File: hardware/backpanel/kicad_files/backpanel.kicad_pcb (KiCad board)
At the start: 2 copper layers, 72 x 19.2 mm, 0 parts

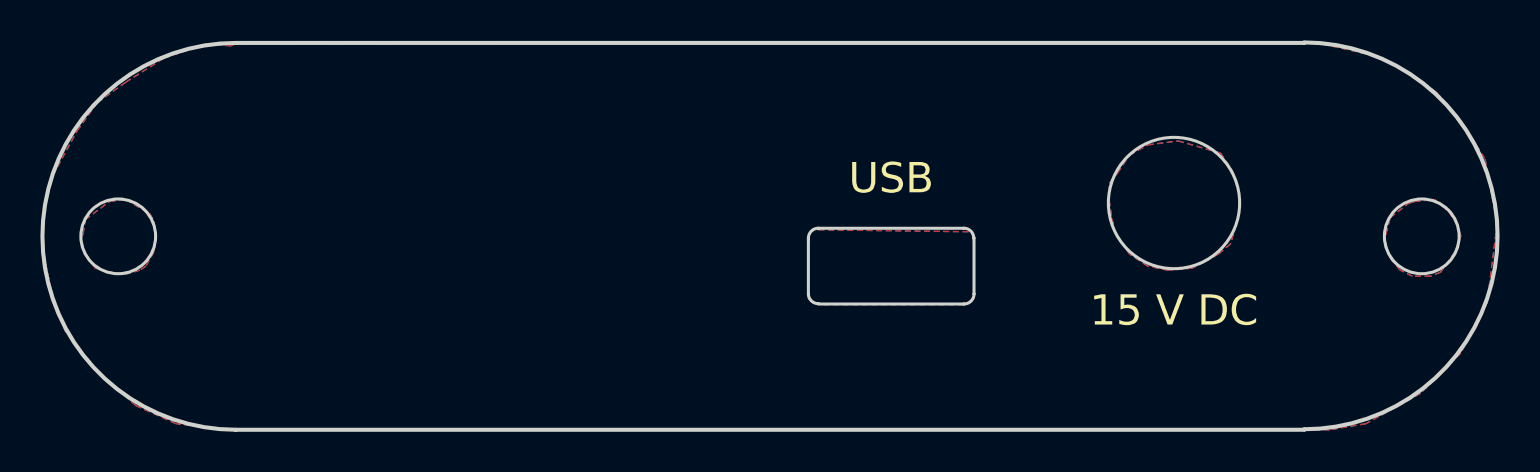
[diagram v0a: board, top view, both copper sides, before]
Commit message: Add files via upload
minor changes to allow KiCad design rules check to complete without errors or warnings
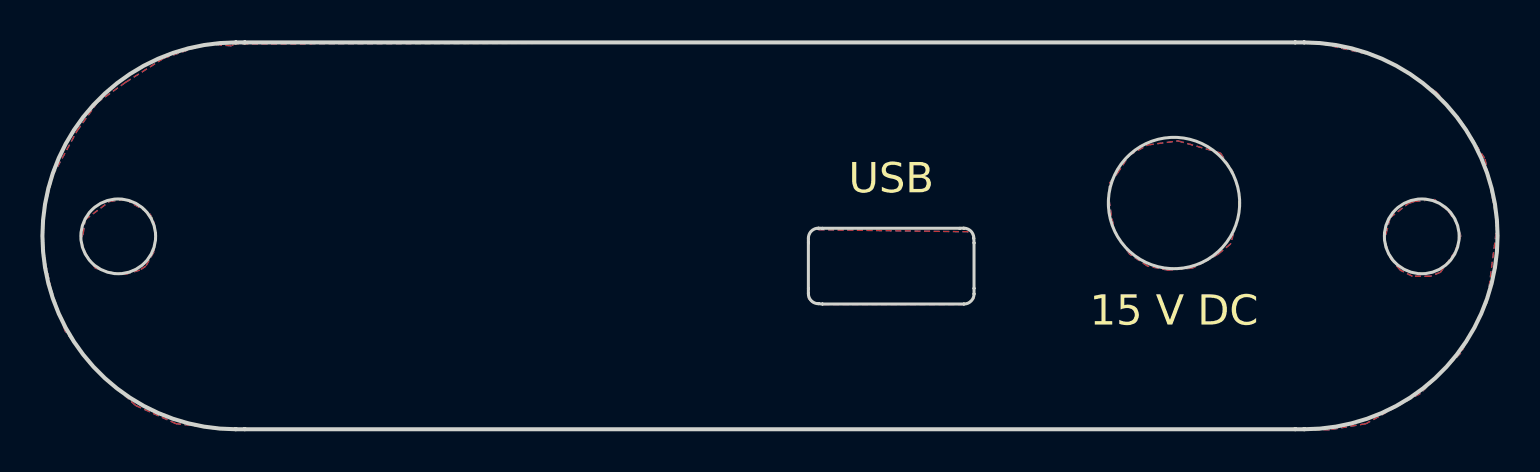
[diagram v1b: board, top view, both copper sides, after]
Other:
- board size 72 x 19.2 mm -> 72 x 19.1 mm
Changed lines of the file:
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@@
   )
   (net 0 "")
-  (gr_arc (start 123.557 100) (mid 113.982 90.425) (end 123.557 80.85) (layer "Edge.Cuts") (width 0.2))
-  (gr_line (start 160.1 90.5) (end 160.1 93.275) (layer "Edge.Cuts") (width 0.15))
-  (gr_line (start 152.4 93.775) (end 159.6 93.775) (layer "Edge.Cuts") (width 0.15))
+  (gr_arc (start 123.557 99.975) (mid 113.982 90.4) (end 123.557 80.825) (layer "Edge.Cuts") (width 0.2))
+  (gr_line (start 160.1 90.75) (end 160.1 93) (layer "Edge.Cuts") (width 0.15))
+  (gr_line (start 152.6 93.775) (end 159.6 93.775) (layer "Edge.Cuts") (width 0.15))
   (gr_arc (start 151.9 90.52) (mid 152.046447 90.166447) (end 152.4 90.02) (layer "Edge.Cuts") (width 0.15))
   (gr_arc (start 152.4 93.76) (mid 152.046447 93.613553) (end 151.9 93.26) (layer "Edge.Cuts") (width 0.15))
   (gr_arc (start 160.1 93.275) (mid 159.953553 93.628553) (end 159.6 93.775) (layer "Edge.Cuts") (width 0.15))
+  (gr_line (start 151.9 93) (end 151.9 93.26) (layer "Edge.Cuts") (width 0.15))
+  (gr_line (start 151.9 90.75) (end 151.9 90.52) (layer "Edge.Cuts") (width 0.15))
   (gr_arc (start 159.59 90.02) (mid 159.943553 90.166447) (end 160.09 90.52) (layer "Edge.Cuts") (width 0.15))
+  (gr_line (start 152.4 90.02) (end 152.6 90.025) (layer "Edge.Cuts") (width 0.15))
+  (gr_line (start 160.09 90.52) (end 160.1 90.75) (layer "Edge.Cuts") (width 0.15))
+  (gr_line (start 176 99.975) (end 176.443 99.975) (layer "Edge.Cuts") (width 0.2))
   (gr_circle (center 170 88.775) (end 173.25 88.775) (layer "Edge.Cuts") (width 0.15) (fill none))
-  (gr_line (start 176.443 80.85) (end 123.557 80.85) (layer "Edge.Cuts") (width 0.2))
-  (gr_line (start 123.557 100) (end 176.443 100) (layer "Edge.Cuts") (width 0.2))
+  (gr_line (start 176 80.825) (end 124 80.825) (layer "Edge.Cuts") (width 0.2))
+  (gr_line (start 124 99.975) (end 176 99.975) (layer "Edge.Cuts") (width 0.2))
+  (gr_line (start 152.4 93.76) (end 152.6 93.775) (layer "Edge.Cuts") (width 0.15))
+  (gr_line (start 159.4 90.025) (end 159.59 90.02) (layer "Edge.Cuts") (width 0.15))
+  (gr_line (start 176 80.825) (end 176.443 80.825) (layer "Edge.Cuts") (width 0.2))
+  (gr_line (start 123.557 99.975) (end 124 99.975) (layer "Edge.Cuts") (width 0.2))
   (gr_circle (center 182.265 90.425) (end 184.115 90.425) (layer "Edge.Cuts") (width 0.15) (fill none))
+  (gr_line (start 160.1 93.275) (end 160.1 93) (layer "Edge.Cuts") (width 0.15))
   (gr_arc (start 176.443 80.825) (mid 186.018 90.4) (end 176.443 99.975) (layer "Edge.Cuts") (width 0.2))
-  (gr_line (start 152.4 90.025) (end 159.6 90.025) (layer "Edge.Cuts") (width 0.15))
-  (gr_line (start 151.9 90.5) (end 151.9 93.275) (layer "Edge.Cuts") (width 0.15))
+  (gr_line (start 152.6 90.025) (end 159.4 90.025) (layer "Edge.Cuts") (width 0.15))
+  (gr_line (start 151.9 90.75) (end 151.9 93) (layer "Edge.Cuts") (width 0.15))
   (gr_circle (center 117.735 90.425) (end 119.585 90.425) (layer "Edge.Cuts") (width 0.15) (fill none))
+  (gr_line (start 123.557 80.825) (end 124 80.825) (layer "Edge.Cuts") (width 0.2))
   (gr_text "15 V DC" (at 170 94.1) (layer "F.SilkS")
     (effects (font (size 1.5 1.5) (thickness 0.2)))
